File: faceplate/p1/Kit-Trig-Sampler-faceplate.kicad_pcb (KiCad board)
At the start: 2 copper layers, 80.9 x 128.5 mm, 26 parts

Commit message: p2 started
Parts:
- removed the G*** at (51.0, 67.4)
- removed the REF** at (51.2, 126.9)
- removed the REF** at (51.0, 7.16)
- added ?: , , F.Cu at (50.8, 7.22)
- added G***: LOGO, artwork:sampler-p1-rev6, F.Cu at (51.2, 67.6)
- added REF**: Rail_Connection_16HP, 4ms_Faceplate:Rail_Connection_16HP, B.Cu at (51.0, 126.8)

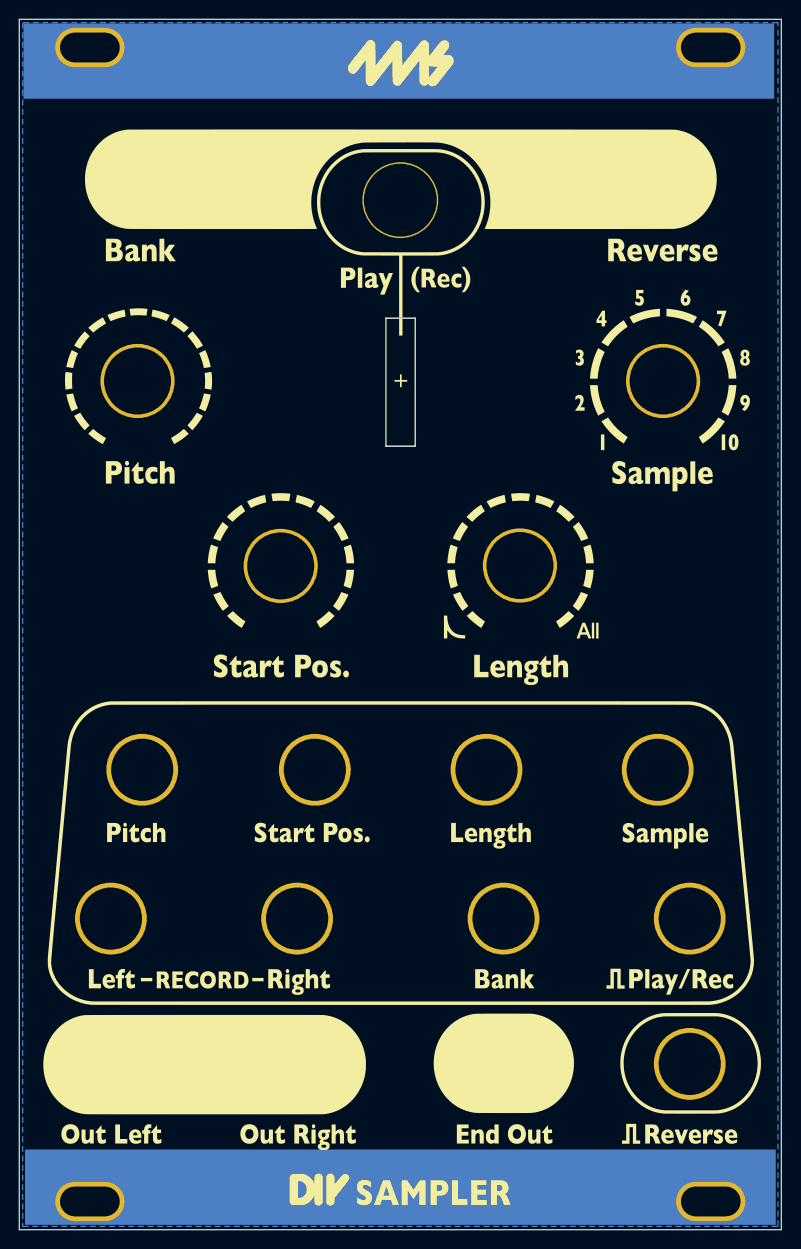
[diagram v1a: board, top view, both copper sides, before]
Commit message: updated p2 faceplate
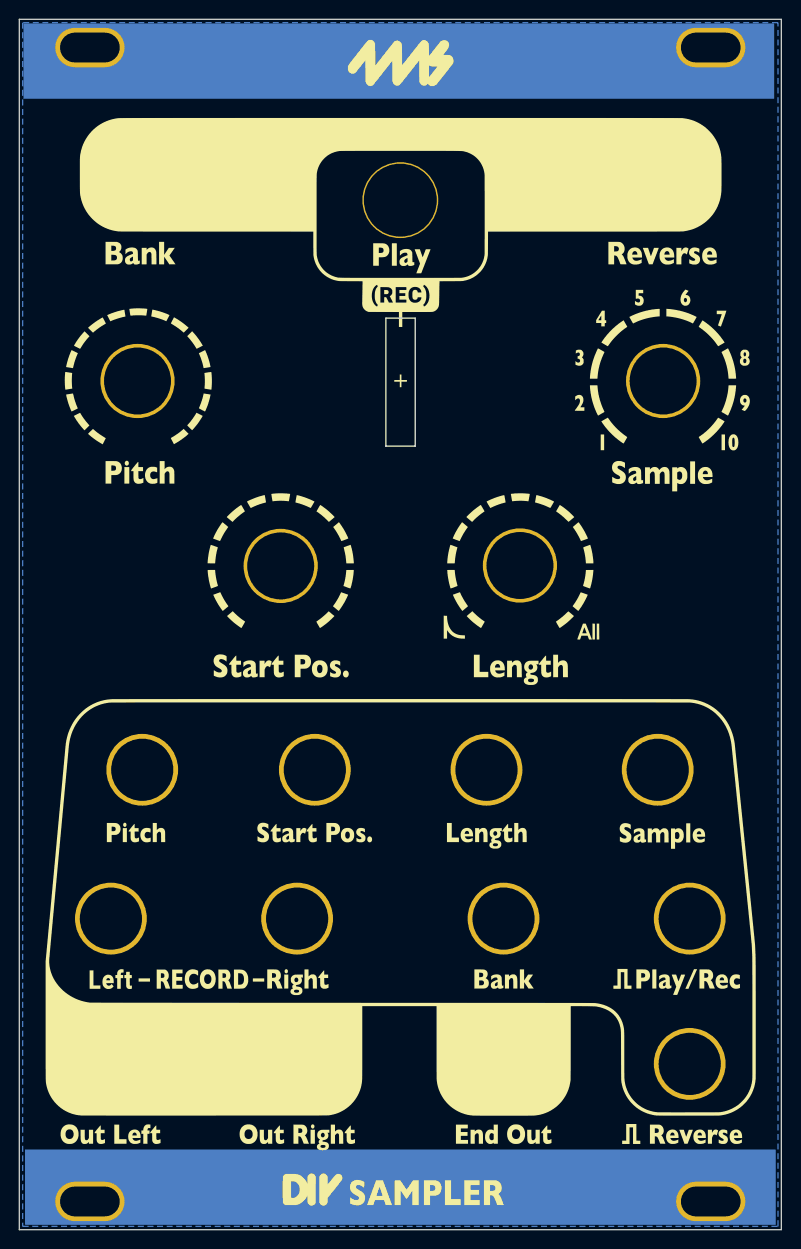
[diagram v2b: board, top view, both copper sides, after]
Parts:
- removed the G*** at (51.2, 67.6)
- added G***: LOGO, artwork:sampler-p2-rev1, F.Cu at (51.0, 67.6)
